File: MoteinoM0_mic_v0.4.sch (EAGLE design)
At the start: 39 parts, among them J1 BNCPTH, J3 GND, J9 MIC_OUT, U1 SPU0410LR5H-QB, U2 OPA1679IRUMT, U3 OPA1677DBVX, U4 APFA3010SEKJ3ZGKQBKC

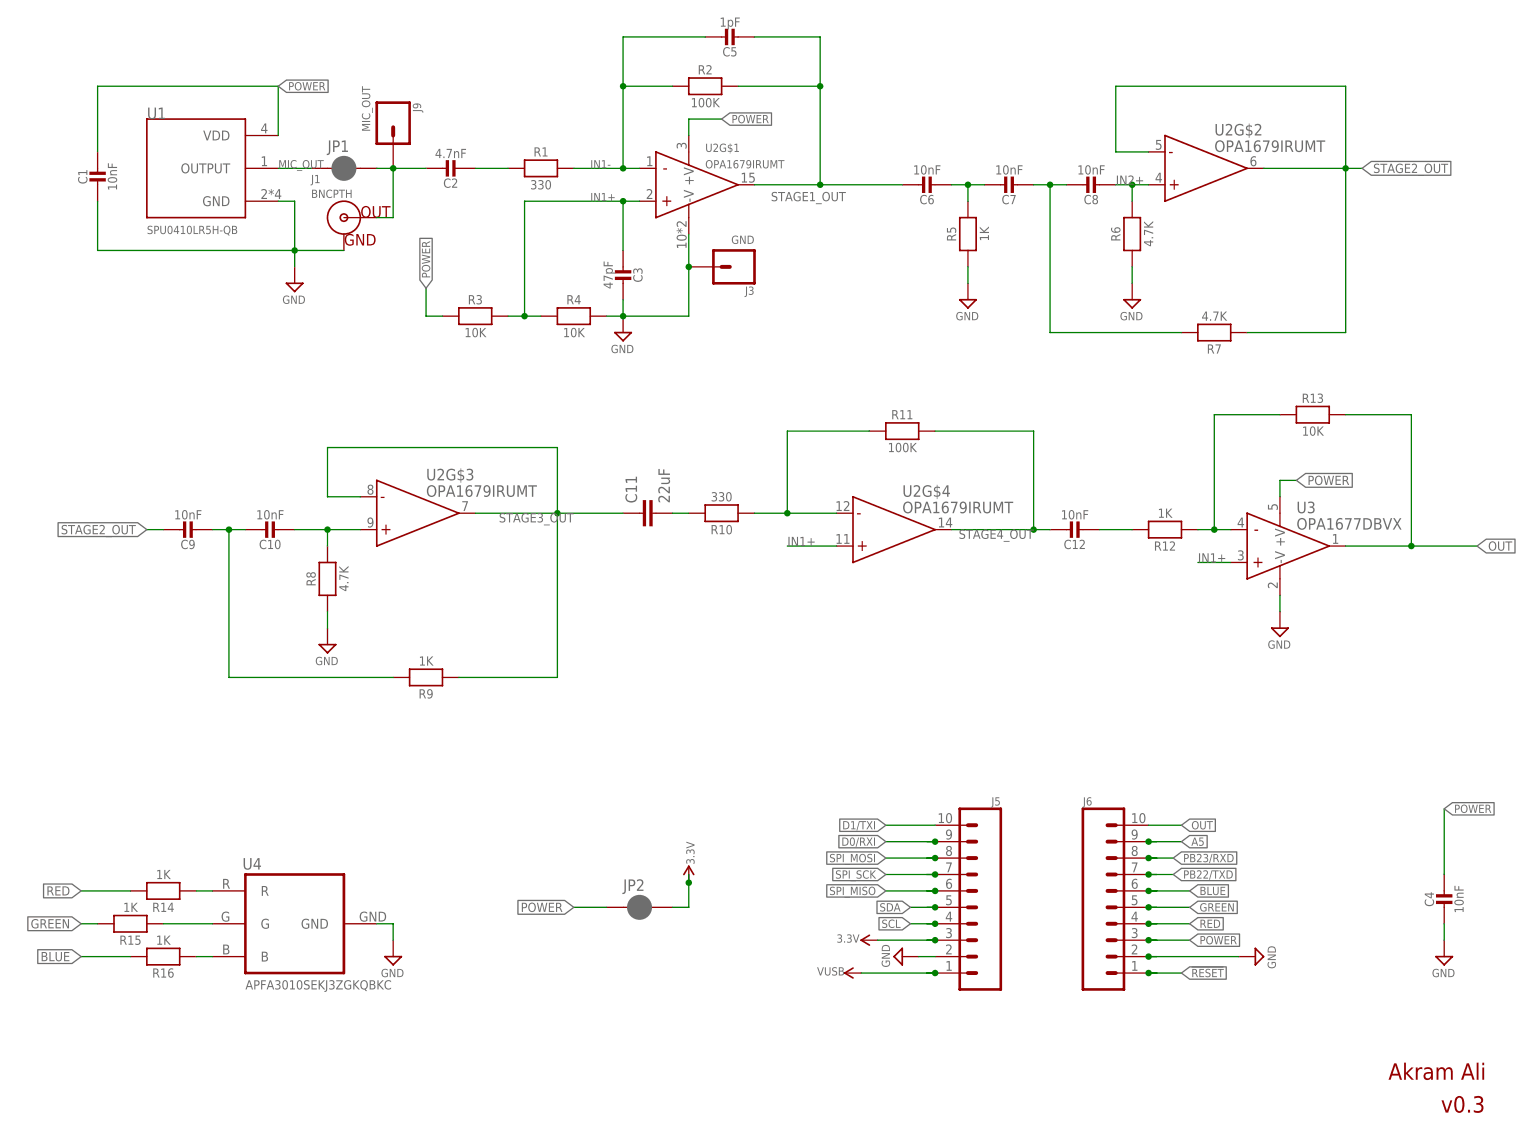
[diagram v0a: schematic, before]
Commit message: v0.4
- removed stage 5
- board size update
- header size increased
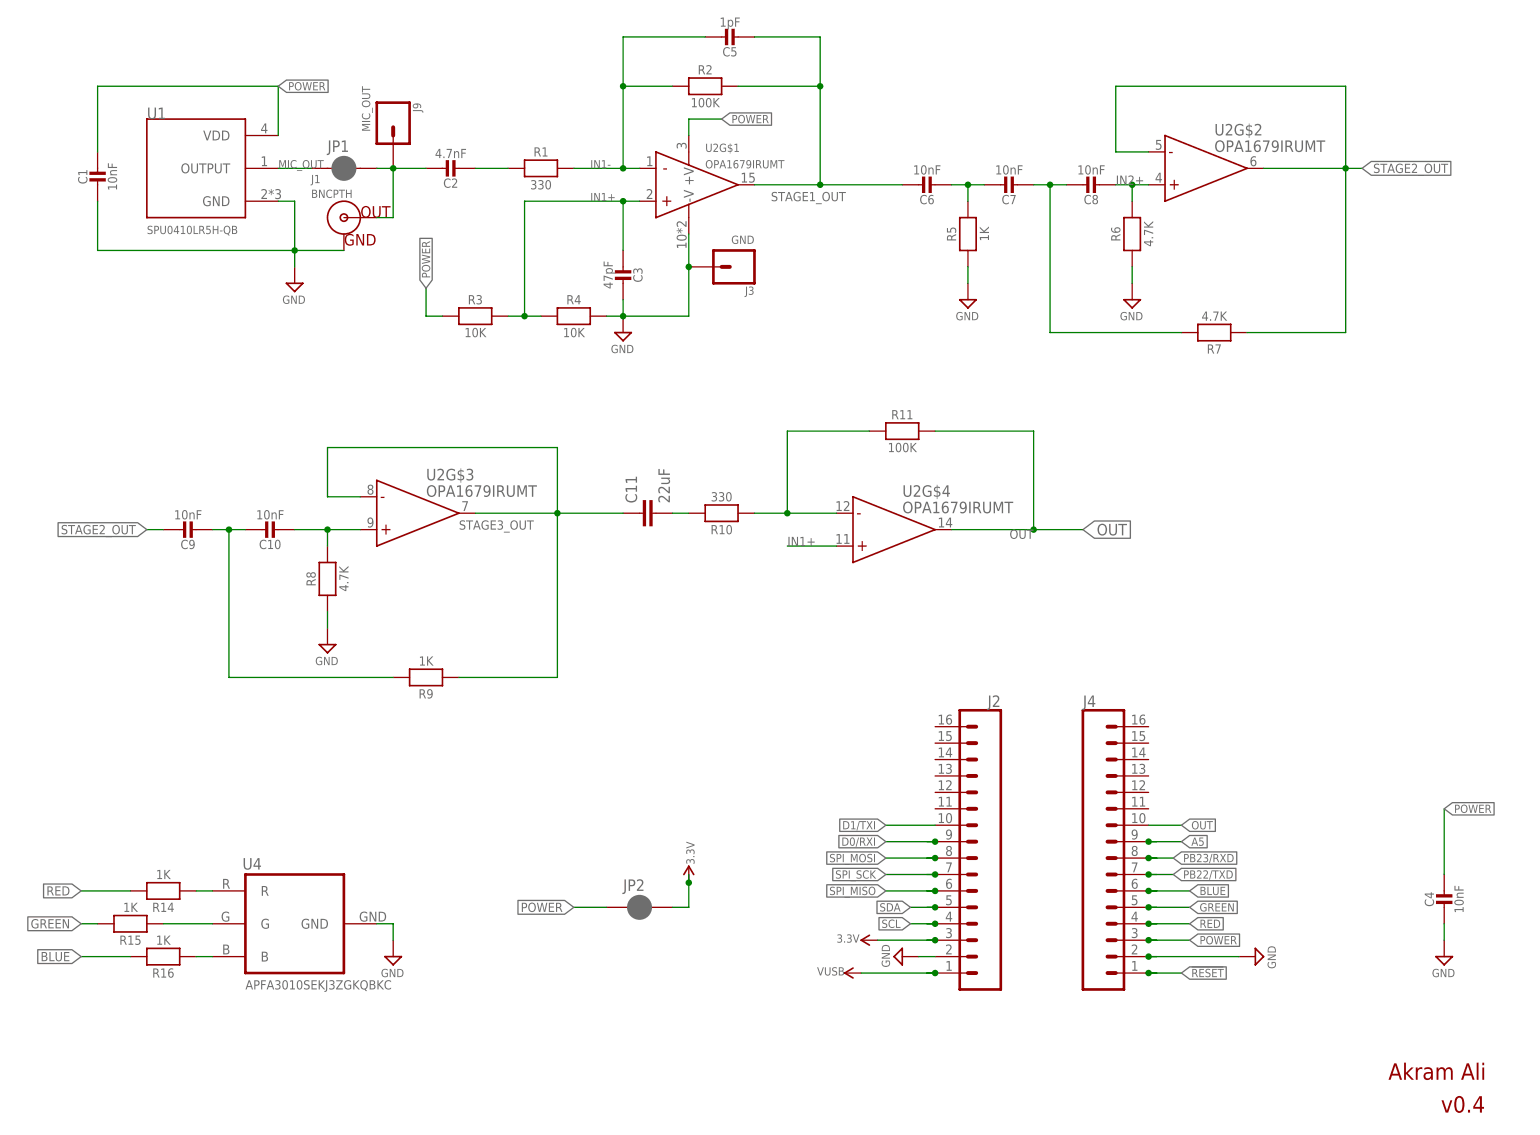
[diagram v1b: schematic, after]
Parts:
- removed C12: 10nF, Adafruit Feather 32u4 Bluefruit LE:MICROBUILDER_CAP_CERAMIC_0402MP
- removed J5, J6: (no value), SparkFun-Connectors:CONN_10NO_SILK_PTH_FEMALE
- removed R12: 1K, Adafruit Feather 32u4 Bluefruit LE:MICROBUILDER_RESISTOR_0402MP
- removed R13: 10K, Adafruit Feather 32u4 Bluefruit LE:MICROBUILDER_RESISTOR_0402MP
- removed U3: OPA1677DBVX, OPA1677DBV:OPA1677DBVX
- added J2, J4: (no value), SparkFun-Connectors:CONN_161X16_NO_SILK
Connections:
- removed net N$17: C12.2, R12.2
- removed net N$18: R12.1, R13.1, U3.-IN
- removed net STAGE4_OUT: C12.1, R11.2, U2G$4.OUT
- net !RESET: now also J4.1; no longer J6.1
- net 3.3V: now also J2.3; no longer J5.3
- net A5: now also J4.9; no longer J6.9
- net BLUE: now also J4.6; no longer J6.6
- net D0/RXI: now also J2.9; no longer J5.9
- net D1/TXI: now also J2.10; no longer J5.10
- net GND: now also J2.2, J4.2; no longer J5.2, J6.2, U3.-V
- net GREEN: now also J4.5; no longer J6.5
- net IN1+: no longer U3.+IN
- net OUT: now also J4.10, R11.2, U2G$4.OUT; no longer J6.10, R13.2, U3.OUT
- net PB22/TXD: now also J4.7; no longer J6.7
- net PB23/RXD: now also J4.8; no longer J6.8
- net POWER: now also J4.3; no longer J6.3, U3.+V
- net RED: now also J4.4; no longer J6.4
- net SCL: now also J2.4; no longer J5.4
- net SDA: now also J2.5; no longer J5.5
- net SPI_MISO: now also J2.6; no longer J5.6
- net SPI_MOSI: now also J2.8; no longer J5.8
- net SPI_SCK: now also J2.7; no longer J5.7
- net VUSB: now also J2.1; no longer J5.1
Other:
- note added: "v0.4"
- note removed: "v0.3"
